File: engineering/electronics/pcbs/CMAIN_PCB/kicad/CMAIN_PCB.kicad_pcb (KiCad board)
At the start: 4 copper layers, 210.2 x 220 mm, 258 parts, among them IC1 TSYS01, J1 RPI_5_WITH_SSQ-120-01-F-D, J10 1778719, J11 M9N-G4-3100, J12 B04B-JWPF-SK-R, J13 B04B-JWPF-SK-R, J14 XT30PW-F, J15 SM04B-GHS-TB_LF__SN_, J16 1778719, J17 SM03B-GHS-TB(LF)(SN), J19 1778719, J2 1778719, J21 1778719, J23 B04B-JWPF-SK-R, J24 1778719, J25 B08B-JWPF-SK-R, J26 B08B-JWPF-SK-R, J27 B04B-JWPF-SK-R, J28 B08B-JWPF-SK-R, J29 B06B-JWPF-SK-R, J3 AXK6S00547YG, J30 B06B-JWPF-SK-R, J31 B06B-JWPF-SK-R, J32 B04B-JWPF-SK-R, J34 B08B-JWPF-SK-R, J35 SM04B-GHS-TB_LF__SN_, J36 SM05B-GHS-TB_LF__SN_, J37 B04B-JWPF-SK-R, J38 B04B-JWPF-SK-R, J39 B04B-JWPF-SK-R, J4 AXK6S00547YG, J40 B04B-JWPF-SK-R, J41 SM06B-GHS-TB_LF__SN_, J42 B08B-JWPF-SK-R, J43 B04B-JWPF-SK-R, J44 B08B-JWPF-SK-R, J45 B04B-JWPF-SK-R, J46 B04B-JWPF-SK-R, J47 GIGABLOX_NANO_SWITCH_REVA_MOD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, J48 B04B-JWPF-SK-R, J49 B04B-JWPF-SK-R, J5 SM04B-GHS-TB_LF__SN_, J50 1778719, J51 GIGABLOX_NANO_SWITCH_REVA_MOD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, J52 B04B-JWPF-SK-R, J53 B04B-JWPF-SK-R, J55 B04B-JWPF-SK-R, J56 B04B-JWPF-SK-R, J57 B04B-JWPF-SK-R, J6 1778719, J7 SM04B-GHS-TB_LF__SN_, J8 B04B-JWPF-SK-R, J9 SM04B-GHS-TB_LF__SN_, K1 CPC1019N, K10 CPC1019N, K2 CPC1019N, K4 CPC1019N, K5 CPC1019N, K6 CPC1019N, K7 CPC1019N, K8 CPC1019N, K9 CPC1019N, Q1 SIRA99DP-T1-GE3, Q2 SIRA99DP-T1-GE3, Q4 PSMN4R3-30BL,118, Q5 PSMN4R3-30BL,118, Q6 PSMN4R3-30BL,118, Q7 PSMN4R3-30BL,118, Q8 PSMN4R3-30BL,118, Q9 PSMN4R3-30BL,118, U1 TJA1049T/3J, U10 SMTSO25100CTJ, U11 SMTSO25100CTJ, U12 SMTSO25100CTJ, U13 SMTWEM245STR, U14 SMTWEM245STR, U15 SMTWEM245STR, U16 SMTWEM245STR, U17 SY8205FCC, U18 SY8205FCC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

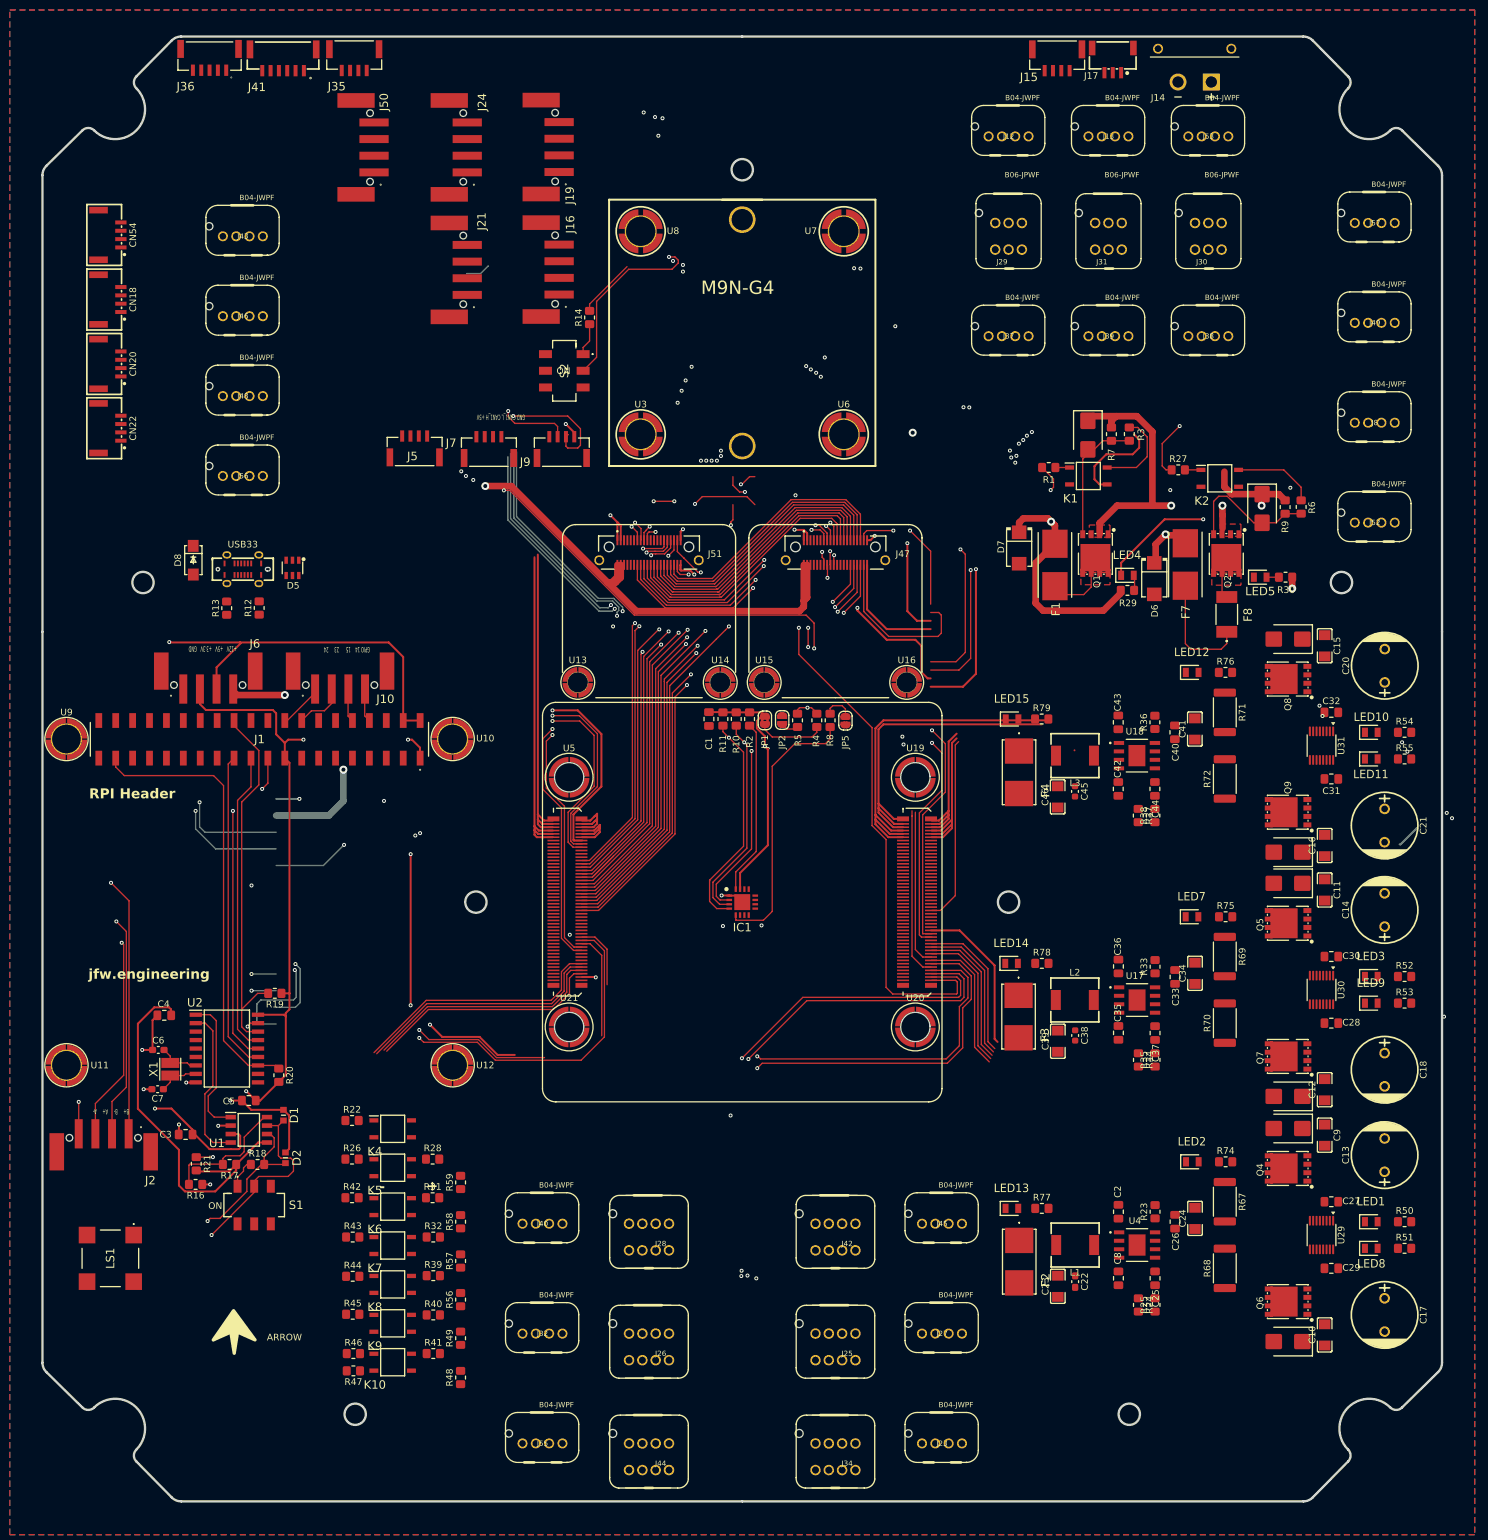
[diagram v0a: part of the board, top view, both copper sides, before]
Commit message: Update CMAIN PCB routing from latest archive
Import Julius's latest CMAIN KiCad update, excluding local .history and backup archives. Remap undefined Rescue footprint graphics to F.Fab so KiCad CLI can load the board, and add KiCad ERC/DRC reports.
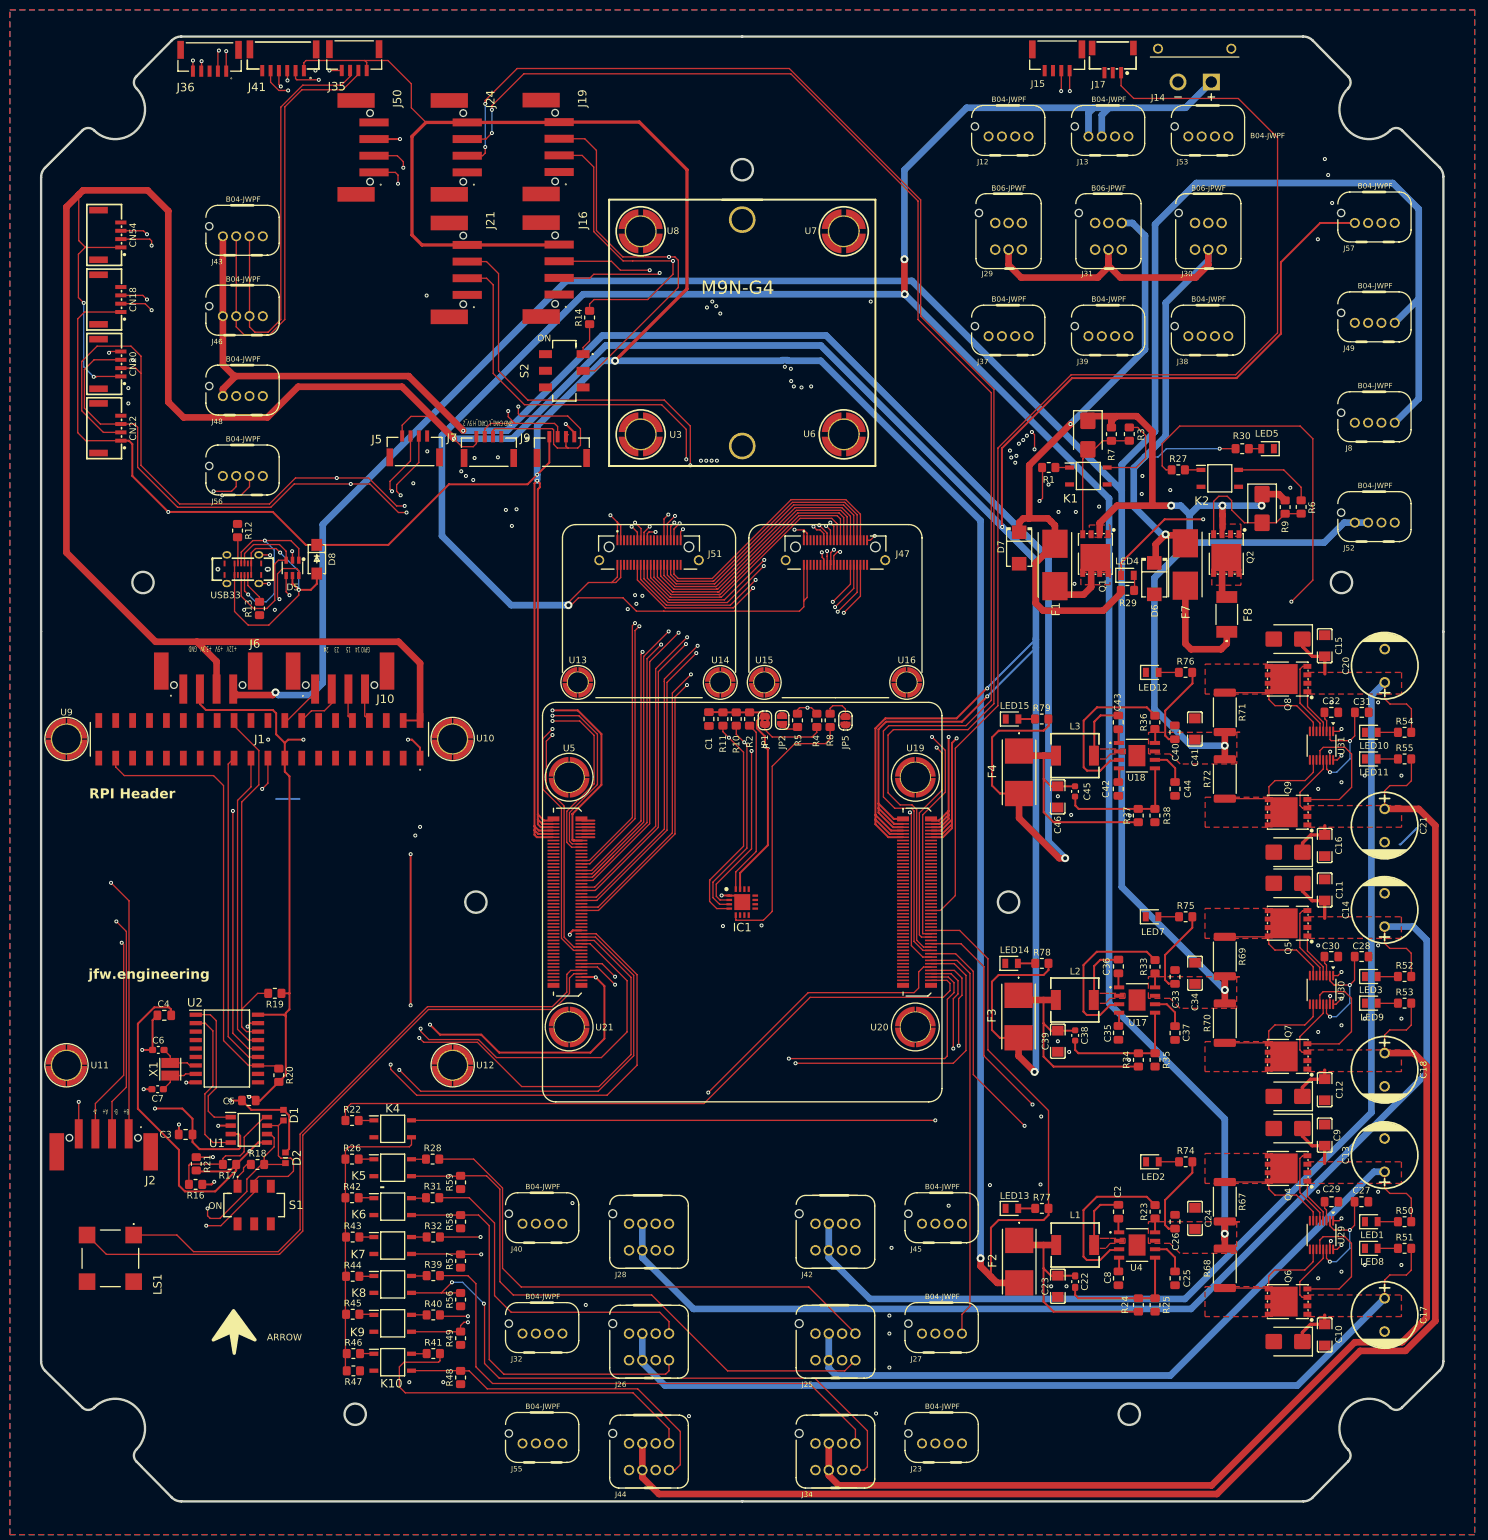
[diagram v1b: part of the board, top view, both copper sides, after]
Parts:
- moved R30 20.4 mm to (275.1, 81.9), turned to 0 degrees
- moved LED5 19.3 mm to (278.9, 81.9), turned to 180 degrees
- moved D8 18.6 mm to (136.1, 98.5)
- moved R12 12.1 mm to (124.2, 94.2), turned to -90 degrees
- moved C31 11.0 mm to (293.1, 121.5)
- moved C28 11.0 mm to (293.0, 158.2)
- moved C29 10.0 mm to (288.5, 195.0)
- moved LED12 6.00 mm to (261.6, 115.5)
- moved LED2 6.00 mm to (261.6, 189.0)
- moved LED7 6.00 mm to (261.5, 152.2)
- moved R74 6.00 mm to (266.6, 189.0)
- moved R75 6.00 mm to (266.6, 152.2)
- moved R76 6.00 mm to (266.6, 115.5)
- moved R13 4.93 mm to (127.5, 105.9)
- moved C27 4.52 mm to (293.0, 195.0)
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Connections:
- J25 pad 5: CANL_DRONE -> CAN1_L
- J25 pad 6: CANH_DRONE -> CAN1_H
- J26 pad 5: CANL_DRONE -> CAN1_L
- J26 pad 6: CANH_DRONE -> CAN1_H
- J28 pad 5: CANL_DRONE -> CAN1_L
- J28 pad 6: CANH_DRONE -> CAN1_H
- J34 pad 5: CANL_DRONE -> CAN1_L
- J34 pad 6: CANH_DRONE -> CAN1_H
- J42 pad 5: CANL_DRONE -> CAN1_L
- J42 pad 6: CANH_DRONE -> CAN1_H
- J44 pad 5: CANL_DRONE -> CAN1_L
- J44 pad 6: CANH_DRONE -> CAN1_H
- R14 pad 1: /CAN2_H -> Net-(S2-NC_1)
- S2 pad 1: /CAN2_H -> Net-(S2-NC_1)
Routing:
- net 5V_1: track 141.3 -> 770.4 mm, vias 1 -> 6
- net 5V_2: track 163.4 -> 784.7 mm, vias 1 -> 8
- net CAN1_H: track 570.2 -> 1029.6 mm, vias 6 -> 12
- net CAN1_L: track 564.6 -> 1020.7 mm, vias 6 -> 12
- net 12V_2: track 8.33 -> 412.2 mm, vias 1 -> 2
- net 12V_1: track 75.0 -> 441.3 mm, vias 1 -> 4
- net 5V_3: track 0.00 -> 264.3 mm, vias 0 -> 2
- net /FMU_CH7: track 21.8 -> 277.9 mm, vias 0 -> 2
- net Net-(D17-C): track 0.00 -> 245.9 mm
- net /N_IO_LED_SAFETY: track 0.00 -> 219.6 mm, vias 1 -> 3
- net /IO_SAFETY_SWITCH_IN: track 9.84 -> 213.7 mm, vias 0 -> 3
- net /FMU_CH5: track 22.2 -> 220.6 mm, vias 0 -> 2
- net /FMU_CH6: track 22.1 -> 217.8 mm, vias 0 -> 2
- net Net-(D14-C): track 0.00 -> 193.2 mm
- net Net-(D16-C): track 0.00 -> 191.5 mm
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- added copper zone on F.Cu, net 12V_2
- added copper zone on F.Cu, net 12V_3
- added copper zone on F.Cu, net Net-(D12-C)
- added copper zone on F.Cu, net Net-(D13-C)
- added copper zone on F.Cu, net Net-(D14-C)
- added copper zone on F.Cu, net Net-(D15-C)
- added copper zone on F.Cu, net Net-(D16-C)
- added copper zone on F.Cu, net Net-(D17-C)
- added copper zone on F.Cu, net Net-(Q4-D)
- added copper zone on F.Cu, net Net-(Q5-D)
- added copper zone on F.Cu, net Net-(Q6-D)
- added copper zone on F.Cu, net Net-(Q7-D)
- added copper zone on F.Cu, net Net-(Q8-D)
- added copper zone on F.Cu, net Net-(Q9-D)
- added copper zone on F.Cu, net Net-(U17-LX)
- added copper zone on F.Cu, net Net-(U18-LX)
- added copper zone on F.Cu, net Net-(U4-LX)
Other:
- board size 210.2 x 220 mm -> 210.6 x 220 mm
- board text added: "GND CAN1_L CAN1_H 5V_2"
- board text removed: "+"
- board text removed: "GND CAN1_L CAN1_H +5V"
